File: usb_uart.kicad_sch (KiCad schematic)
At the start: 12 parts

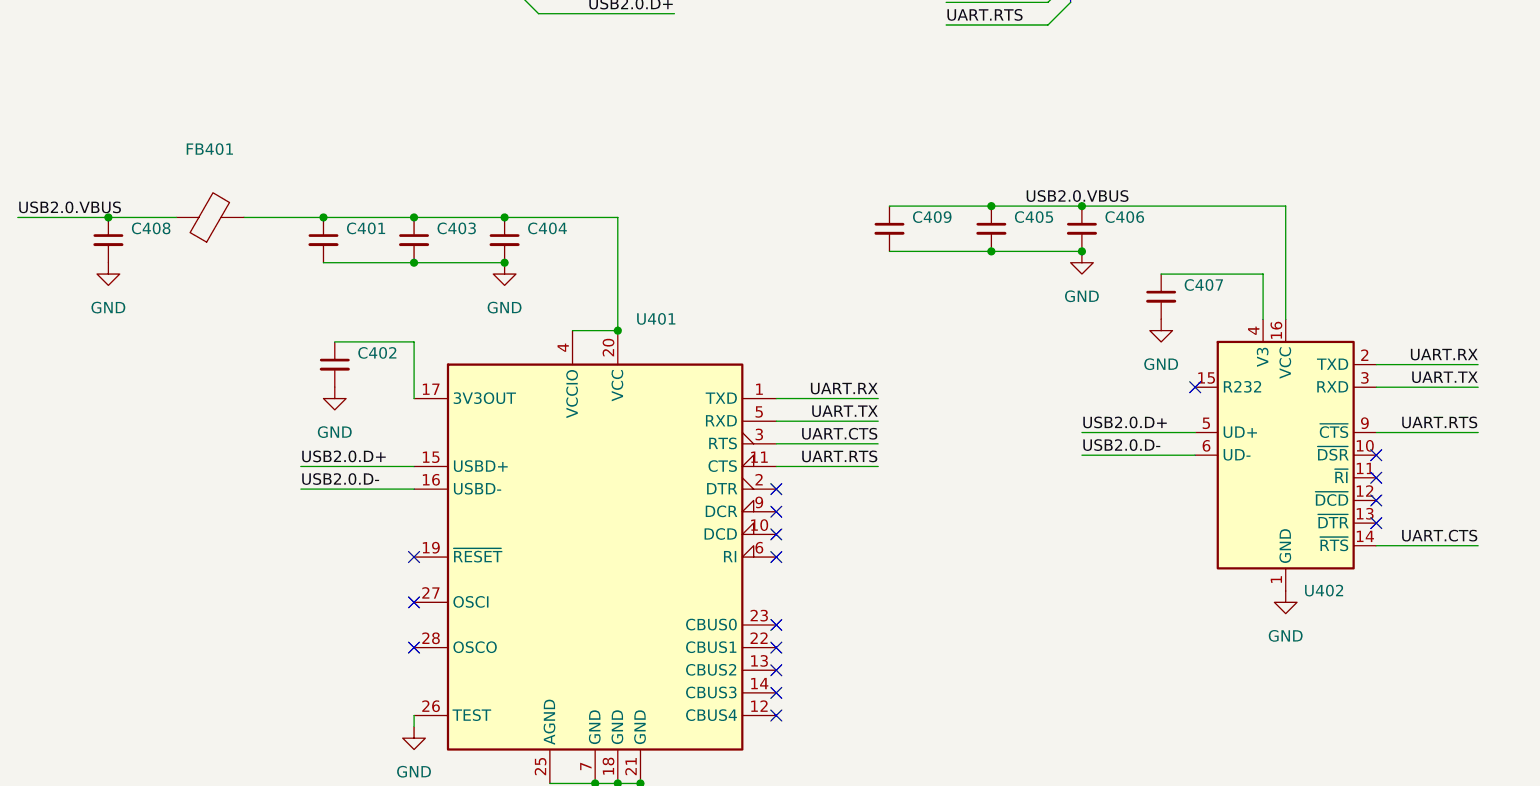
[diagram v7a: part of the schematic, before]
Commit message: Reduce trace resistance of 10mOhm channel
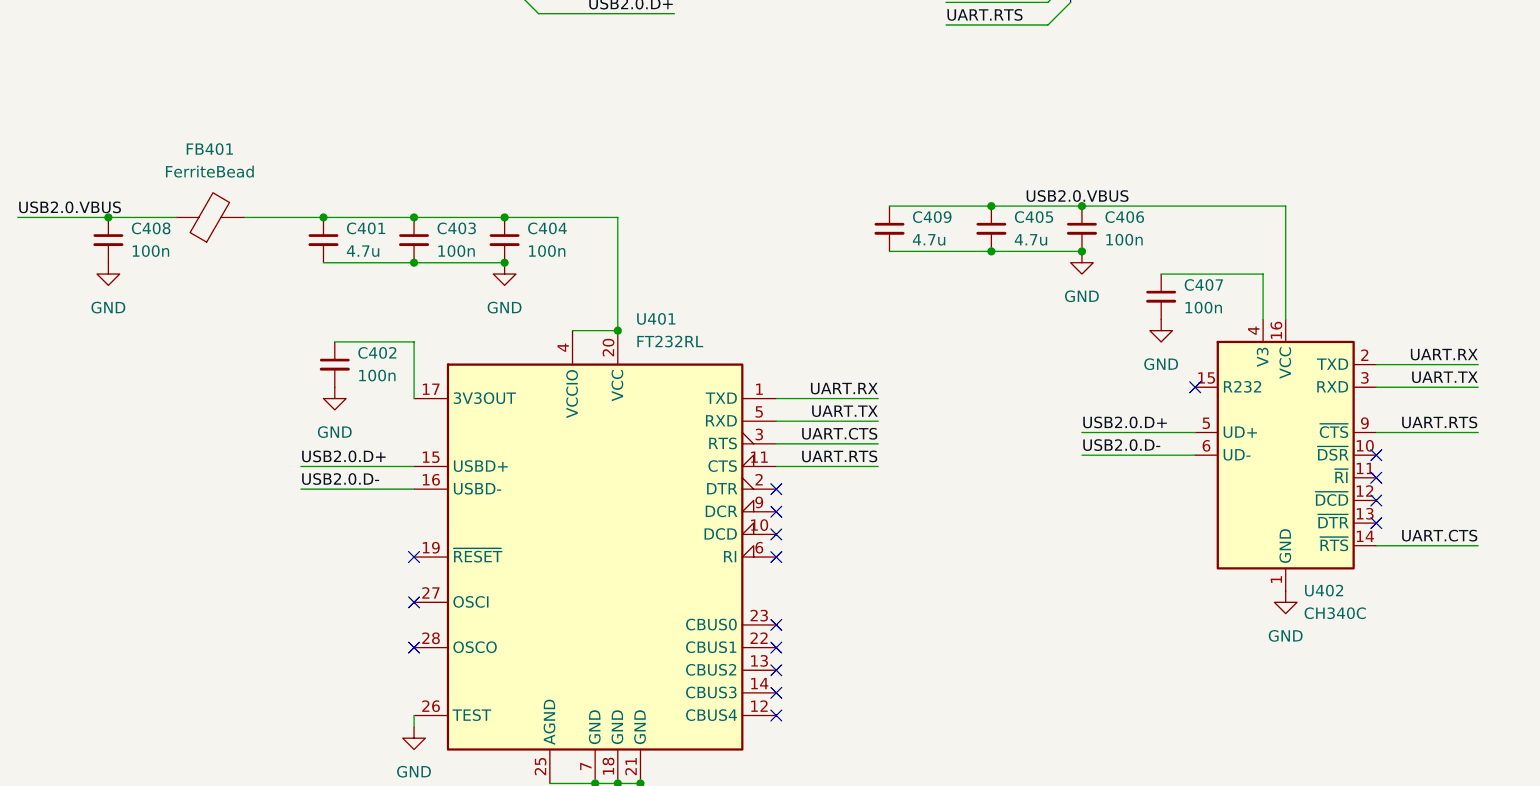
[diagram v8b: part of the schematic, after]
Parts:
- C401, C405, C409: value (none) -> 4.7u; footprint (none) -> Capacitor_SMD:C_0805_2012Metric
- C402, C403, C404, C406, C407, C408: value (none) -> 100n; footprint (none) -> Capacitor_SMD:C_0402_1005Metric
- FB401: value (none) -> FerriteBead; footprint (none) -> Inductor_SMD:L_0805_2012Metric
- U401: value (none) -> FT232RL; footprint (none) -> Package_SO:SSOP-28_5.3x10.2mm_P0.65mm
- U402: value (none) -> CH340C; footprint (none) -> Package_SO:SOIC-16_3.9x9.9mm_P1.27mm
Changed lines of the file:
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@@
       (effects (font (size 1.27 1.27)) (justify left))
     )
-    (property "Value" "" (id 1) (at 76.2 88.9062 0)
-      (effects (font (size 1.27 1.27)) (justify left))
-    )
-    (property "Footprint" "" (id 2) (at 73.66 87.63 0)
+    (property "Value" "100n" (id 1) (at 76.2 88.9062 0)
+      (effects (font (size 1.27 1.27)) (justify left))
+    )
+    (property "Footprint" "Capacitor_SMD:C_0402_1005Metric" (id 2) (at 73.66 87.63 0)
       (effects (font (size 1.27 1.27)) hide)
     )
@@
       (effects (font (size 1.27 1.27)) (justify left))
     )
-    (property "Value" "" (id 1) (at 107.4294 85.09 0)
-      (effects (font (size 1.27 1.27)) (justify left))
-    )
-    (property "Footprint" "" (id 2) (at 130.81 132.08 0)
+    (property "Value" "FT232RL" (id 1) (at 107.4294 85.09 0)
+      (effects (font (size 1.27 1.27)) (justify left))
+    )
+    (property "Footprint" "Package_SO:SSOP-28_5.3x10.2mm_P0.65mm" (id 2) (at 130.81 132.08 0)
       (effects (font (size 1.27 1.27)) hide)
     )
@@
       (effects (font (size 1.27 1.27)) (justify left))
     )
-    (property "Value" "" (id 1) (at 182.3594 115.57 0)
-      (effects (font (size 1.27 1.27)) (justify left))
-    )
-    (property "Footprint" "" (id 2) (at 181.61 111.76 0)
+    (property "Value" "CH340C" (id 1) (at 182.3594 115.57 0)
+      (effects (font (size 1.27 1.27)) (justify left))
+    )
+    (property "Footprint" "Package_SO:SOIC-16_3.9x9.9mm_P1.27mm" (id 2) (at 181.61 111.76 0)
       (effects (font (size 1.27 1.27)) (justify left) hide)
     )
@@
       (effects (font (size 1.27 1.27)) (justify left))
     )
-    (property "Value" "" (id 1) (at 85.09 74.9362 0)
-      (effects (font (size 1.27 1.27)) (justify left))
-    )
-    (property "Footprint" "" (id 2) (at 82.55 73.66 0)
+    (property "Value" "100n" (id 1) (at 85.09 74.9362 0)
+      (effects (font (size 1.27 1.27)) (justify left))
+    )
+    (property "Footprint" "Capacitor_SMD:C_0402_1005Metric" (id 2) (at 82.55 73.66 0)
       (effects (font (size 1.27 1.27)) hide)
     )
@@
       (effects (font (size 1.27 1.27)) (justify left))
     )
-    (property "Value" "" (id 1) (at 168.91 81.2862 0)
-      (effects (font (size 1.27 1.27)) (justify left))
-    )
-    (property "Footprint" "" (id 2) (at 166.37 80.01 0)
+    (property "Value" "100n" (id 1) (at 168.91 81.2862 0)
+      (effects (font (size 1.27 1.27)) (justify left))
+    )
+    (property "Footprint" "Capacitor_SMD:C_0402_1005Metric" (id 2) (at 166.37 80.01 0)
       (effects (font (size 1.27 1.27)) hide)
     )
@@
       (effects (font (size 1.27 1.27)) (justify left))
     )
-    (property "Value" "" (id 1) (at 149.86 73.6662 0)
-      (effects (font (size 1.27 1.27)) (justify left))
-    )
-    (property "Footprint" "" (id 2) (at 147.32 72.39 0)
+    (property "Value" "4.7u" (id 1) (at 149.86 73.6662 0)
+      (effects (font (size 1.27 1.27)) (justify left))
+    )
+    (property "Footprint" "Capacitor_SMD:C_0805_2012Metric" (id 2) (at 147.32 72.39 0)
       (effects (font (size 1.27 1.27)) hide)
     )
@@
       (effects (font (size 1.27 1.27)) (justify left))
     )
-    (property "Value" "" (id 1) (at 138.43 73.6662 0)
-      (effects (font (size 1.27 1.27)) (justify left))
-    )
-    (property "Footprint" "" (id 2) (at 135.89 72.39 0)
+    (property "Value" "4.7u" (id 1) (at 138.43 73.6662 0)
+      (effects (font (size 1.27 1.27)) (justify left))
+    )
+    (property "Footprint" "Capacitor_SMD:C_0805_2012Metric" (id 2) (at 135.89 72.39 0)
       (effects (font (size 1.27 1.27)) hide)
     )
@@
       (effects (font (size 1.27 1.27)) (justify left))
     )
-    (property "Value" "" (id 1) (at 160.02 73.6662 0)
-      (effects (font (size 1.27 1.27)) (justify left))
-    )
-    (property "Footprint" "" (id 2) (at 157.48 72.39 0)
+    (property "Value" "100n" (id 1) (at 160.02 73.6662 0)
+      (effects (font (size 1.27 1.27)) (justify left))
+    )
+    (property "Footprint" "Capacitor_SMD:C_0402_1005Metric" (id 2) (at 157.48 72.39 0)
       (effects (font (size 1.27 1.27)) hide)
     )
@@
       (effects (font (size 1.27 1.27)) (justify left))
     )
-    (property "Value" "" (id 1) (at 95.25 74.9362 0)
-      (effects (font (size 1.27 1.27)) (justify left))
-    )
-    (property "Footprint" "" (id 2) (at 92.71 73.66 0)
+    (property "Value" "100n" (id 1) (at 95.25 74.9362 0)
+      (effects (font (size 1.27 1.27)) (justify left))
+    )
+    (property "Footprint" "Capacitor_SMD:C_0402_1005Metric" (id 2) (at 92.71 73.66 0)
       (effects (font (size 1.27 1.27)) hide)
     )
@@
       (effects (font (size 1.27 1.27)) (justify left))
     )
-    (property "Value" "" (id 1) (at 50.8 74.9362 0)
-      (effects (font (size 1.27 1.27)) (justify left))
-    )
-    (property "Footprint" "" (id 2) (at 48.26 73.66 0)
+    (property "Value" "100n" (id 1) (at 50.8 74.9362 0)
+      (effects (font (size 1.27 1.27)) (justify left))
+    )
+    (property "Footprint" "Capacitor_SMD:C_0402_1005Metric" (id 2) (at 48.26 73.66 0)
       (effects (font (size 1.27 1.27)) hide)
     )
@@
       (effects (font (size 1.27 1.27)) (justify left))
     )
-    (property "Value" "" (id 1) (at 74.93 74.9362 0)
-      (effects (font (size 1.27 1.27)) (justify left))
-    )
-    (property "Footprint" "" (id 2) (at 72.39 73.66 0)
+    (property "Value" "4.7u" (id 1) (at 74.93 74.9362 0)
+      (effects (font (size 1.27 1.27)) (justify left))
+    )
+    (property "Footprint" "Capacitor_SMD:C_0805_2012Metric" (id 2) (at 72.39 73.66 0)
       (effects (font (size 1.27 1.27)) hide)
     )
@@
     (in_bom yes) (on_board yes) (fields_autoplaced)
     (property "Reference" "FB401" (id 0) (at 59.6392 63.5 90))
-    (property "Value" "" (id 1) (at 59.6392 66.04 90))
-    (property "Footprint" "" (id 2) (at 59.69 72.898 90)
-      (effects (font (size 1.27 1.27)) hide)
-    )
+    (property "Value" "FerriteBead" (id 1) (at 59.6392 66.04 90))
+    (property "Footprint" "Inductor_SMD:L_0805_2012Metric" (id 2) (at 59.69 72.898 90)
+      (effects (font (size 1.27 1.27)) hide)
+    )
